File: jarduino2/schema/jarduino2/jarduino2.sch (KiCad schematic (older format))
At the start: 52 parts, among them J1 Alimentations 12V, J2 Cmd Mcu, J3 Commandes, J4 Pompe1, J5 Pompe 2, J6 Ext, J8 Program, J9 Tests, Q1 Q_NPN_BCE, Q2 Q_NPN_BCE, SW1 SW_Push, U1 R-78B3.3-2.0, U2 MSP430F1222IDW, U3 RtcArduino

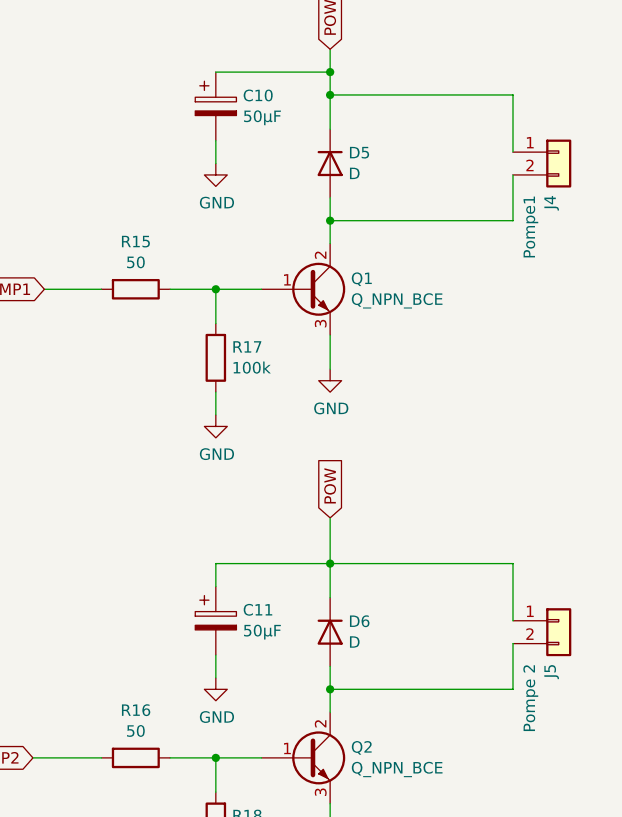
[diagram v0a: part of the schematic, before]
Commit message: Amélioration proto: - Diametre trous de fixation 4mm (avec compo sepcial) - SW1/SW2 echanges Batt/Sol
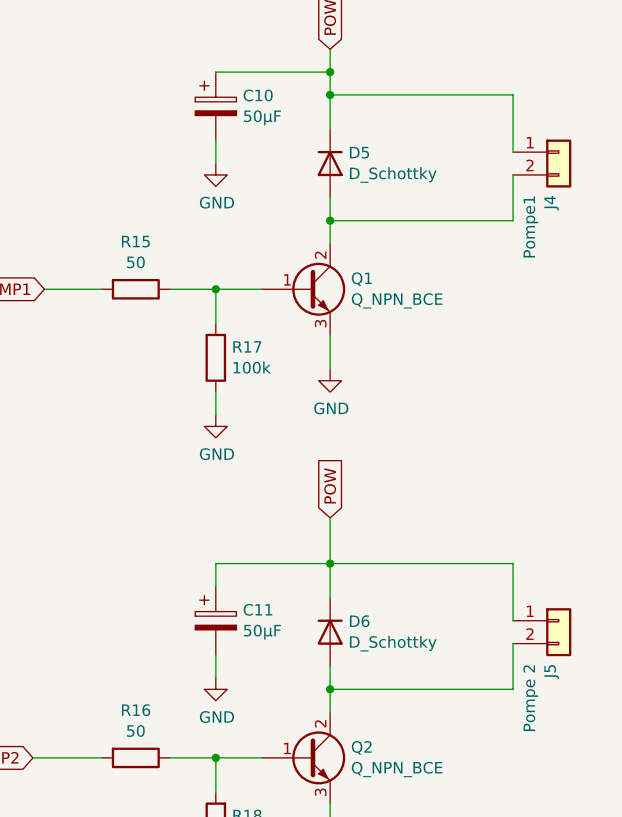
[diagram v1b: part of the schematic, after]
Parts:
- BT1, BT2: RefBpc (none) -> BPC100
- C1, C6, C9: RefBpc (none) -> BPC203
- C10, C11: footprint Capacitor_SMD:C_Elec_4x5.8 -> Capacitor_SMD:CP_Elec_8x6.5; RefBpc (none) -> BPC204
- C2, C4, C5, C7, C8: RefBpc (none) -> BPC202
- C3: footprint Capacitor_SMD:C_1206_3216Metric -> Capacitor_SMD:CP_Elec_6.3x7.7; RefBpc (none) -> BPC201
- D1, D2, D3, D4: footprint Diode_SMD:D_1210_3225Metric -> Diode_SMD:D_SOD-323; RefBpc (none) -> BPC401
- D5, D6: value D -> D_Schottky; footprint Diode_SMD:D_1210_3225Metric -> Diode_SMD:D_SOD-323; RefBpc (none) -> BPC401
- J1: RefBpc (none) -> BPC501
- J2: RefBpc (none) -> BPC502
- J3: RefBpc (none) -> BPC503
- J4: RefBpc (none) -> BPC504
- J5: RefBpc (none) -> BPC505
- J6: RefBpc (none) -> BPC506
- J8: RefBpc (none) -> BPC507
- J9: RefBpc (none) -> BPC508
- L1: RefBpc (none) -> BPC601
- Q1, Q2: RefBpc (none) -> BPC701
- R1: footprint Resistor_SMD:R_0805_2012Metric -> Resistor_SMD:R_0805_2012Metric_Pad1.20x1.40mm_HandSolder; RefBpc (none) -> BPC301
- R10, R12, R13, R14, R9: RefBpc (none) -> BPC303
- R11, R17, R18, R3, R5, R6, R7, R8: RefBpc (none) -> BPC301
- R15, R16: RefBpc (none) -> BPC304
- R2: footprint Resistor_SMD:R_0805_2012Metric -> Resistor_SMD:R_0805_2012Metric_Pad1.20x1.40mm_HandSolder; RefBpc (none) -> BPC302
- R4: RefBpc (none) -> BPC302
- SW1: RefBpc (none) -> BPC101
- U1: RefBpc (none) -> BPC801
- U2: RefBpc (none) -> BPC901
- U3: RefBpc (none) -> BPC802
